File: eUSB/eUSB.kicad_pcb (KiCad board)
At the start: 2 copper layers, 15.6 x 47.6 mm, 8 parts, among them J1 eUSB Connector, J2 USB_A Male

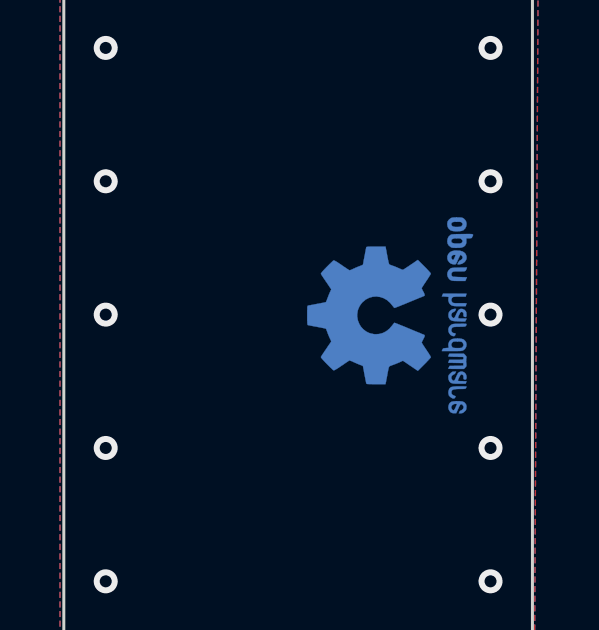
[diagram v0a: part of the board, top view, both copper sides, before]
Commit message: updated silkscrean
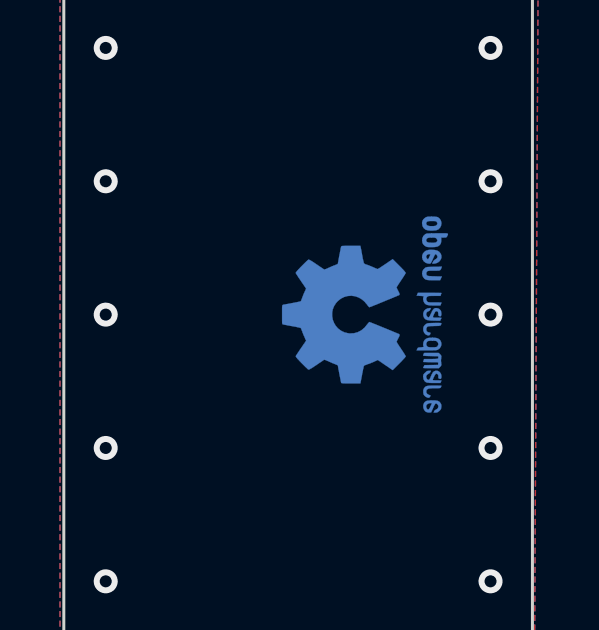
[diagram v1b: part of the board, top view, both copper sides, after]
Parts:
- moved REF** 0.84 mm to (162.2, 73.5)
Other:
- board text added: "eUSB Adapter V.2 January 2025"
- board text removed: "eUSB Adapter V.2 Created for NHS Cisco January 2025"
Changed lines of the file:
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@@
   )
   (footprint "Symbol:OSHW-Logo2_7.3x6mm_Copper" (layer "B.Cu")
-    (at 163.0172 73.5584 -90)
+    (at 162.179 73.533 -90)
     (descr "Open Source Hardware Symbol")
     (tags "Logo Symbol OSHW")
@@
   (gr_line (start 153.543 90.297) (end 166.497 84.963) (layer "User.7") (width 0.15))
   (gr_line (start 166.497 90.297) (end 153.543 90.297) (layer "User.7") (width 0.15))
-  (gr_text "eUSB Adapter V.2\nCreated for NHS Cisco\nJanuary 2025" (at 156.972 73.6092 90) (layer "B.SilkS")
+  (gr_text "eUSB Adapter V.2\nJanuary 2025" (at 155.829 73.6092 90) (layer "B.SilkS")
     (effects (font (size 1 1) (thickness 0.15)) (justify mirror))
   )
